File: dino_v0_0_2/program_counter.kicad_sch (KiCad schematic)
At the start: 20 parts, among them U1 74LS193, U10 74LS02, U11 74LS245, U12 74LS245, U13 74LS245, U14 74LS245, U2 74LS193, U3 74LS193, U36 7400, U4 74LS193

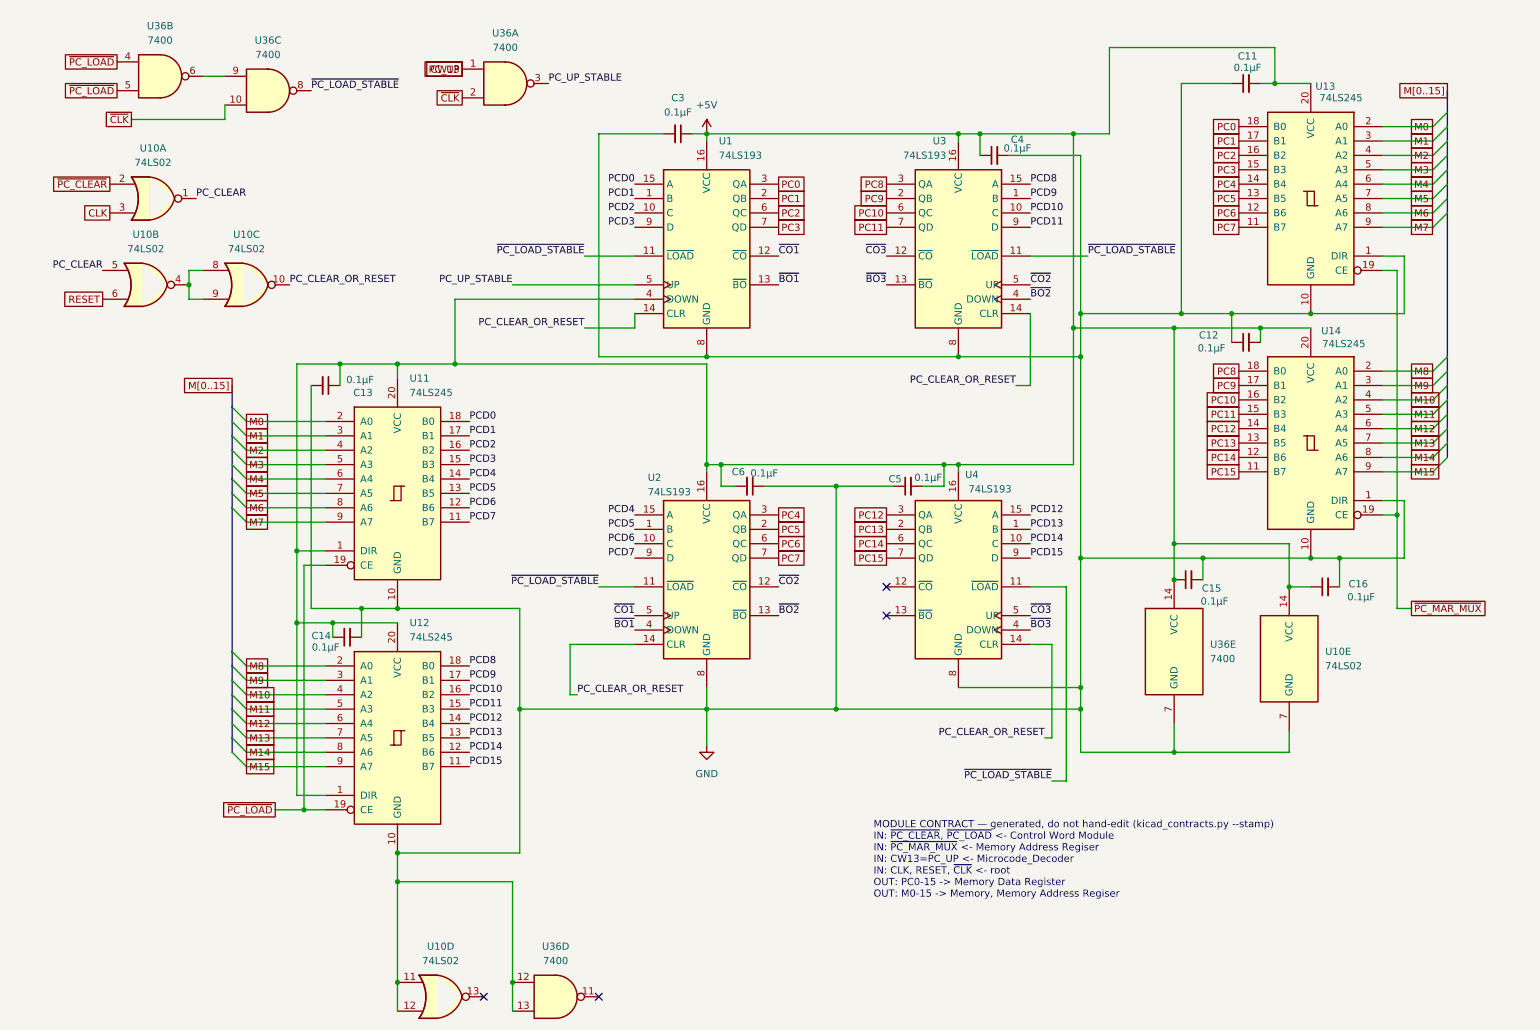
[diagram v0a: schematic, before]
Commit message: feat(int): draw the interrupt block; sheet cleanup pass
New sheet dino_v0_0_2/interrupt.kicad_sch (page 15): U80-U87, R28 4.7k
pull-up on ~{IRQ}, R29 100R on the block's CLK branch, C83-C90. Every
pin per PHASE_INT SECTION 3, checked against the plan with kicad_netlist
and kicad-cli (146 pins, 0 mismatches).

Old sheets (SECTION 3.2): U28.4 lifted off GND to INJECT; U61.3 to
END_OR_ACCEPT; U36.1 to PC_UP_GATED; U49 D0-3 cut from U48 Za-Zd and
routed through U87 as FLAG_NEXT0-3 / FLAG_D0-3; FLAG_C/Z/V/N and the
five decoder outputs made global. dino_serial: U104 74LS05, INTR ->
~{IRQ}, C4.

Placement pass on every sheet: bus entries and global labels no longer
share wires; M, CW, T, IRB and SA buses kept as labelled keys. Nets
diffed against HEAD per sheet: only the intended changes and a rotated
C29. Project ERC: 0 errors. MODULE CONTRACT stamps regenerated.

Co-Authored-By: Claude Fable 5.1 <noreply@anthropic.com>
Claude-Session: https://claude.ai/code/session_01JGxSS4MVUcaZdKZGtKroSg
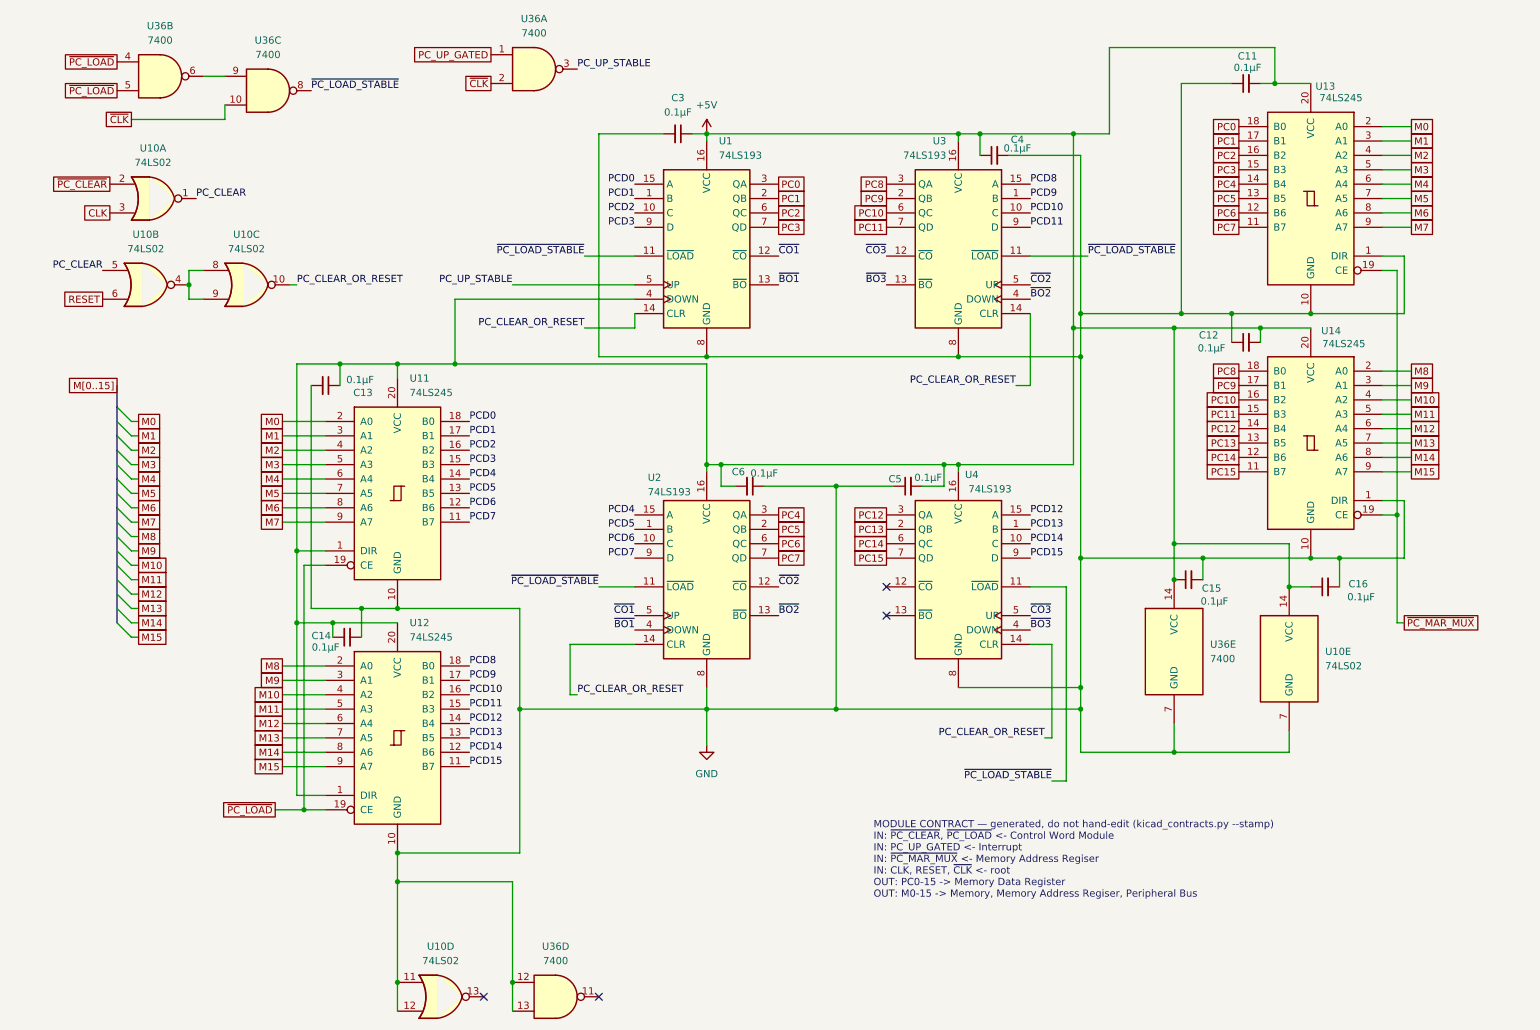
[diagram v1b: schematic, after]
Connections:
- net CW13 renamed PC_UP_GATED
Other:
- note added: "MODULE CONTRACT — generated, do not hand-edit (kicad_contracts.py --stamp) IN: ~{PC_CLEAR}, ~{PC_LOAD} <- Control Word Module IN: PC_UP_GATED <- Interrupt IN: ~{PC_MAR_MUX} <- Memory Address Regiser IN: CLK, RESET, ~{CLK} <- root OUT: PC0-15 -> Memory Data Register OUT: M0-15 -> Memory, Memory Address Regiser, Peripheral Bus"
- note removed: "MODULE CONTRACT — generated, do not hand-edit (kicad_contracts.py --stamp) IN: ~{PC_CLEAR}, ~{PC_LOAD} <- Control Word Module IN: ~{PC_MAR_MUX} <- Memory Address Regiser IN: CW13=PC_UP <- Microcode_Decoder IN: CLK, RESET, ~{CLK} <- root OUT: PC0-15 -> Memory Data Register OUT: M0-15 -> Memory, Memory Address Regiser"
- moved on the sheet: U36A

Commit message: feat(pcb): Rev 1.0 pre-order batch, debug access, no fuse
From the five-way pre-order review:

- Debug: J14 clock select at U27.3 (1.024 MHz / 512k / 256k / 128k /
  STEP), STEP debounced from SW3 through the spare U56 5->6 Schmitt;
  J15 LA header (16 control signals, a GND beside each); J16 power for
  the OB LEDs; DNP cap pads C94/C95/C96 on CLK at U6.2, CLK_ALU at
  U47.11 and CW15 (HALT) at U61.5; 15 GND scope loops so every IC but
  two is within 50 mm of one, plus a +5V test point.
- Power: F1 removed, no fuse (Rico); J9's +5V solid to the plane;
  bulk C97-C100 100 uF spread across the board; C92 ceramic.
- Layout: U6 beside U27 (its CLK pin was 138 mm out on raw CLK), C1/R1
  beside U56, RST_SIG in RESET and CLK_R / CLK_INT / CLK_M / CLK_SEL in
  CLK, thermal gap 0.3 mm (GND plane slots from 25 mm to under 8 mm),
  tracks >= 0.2 mm with no neckdown (6/6 mil tier), board min track rule.
- Values to match the bench: U56 SN7414N, U36 74LS00, U51 DM7400N,
  Y1 4.096 MHz.
- Edge socket: silk outline and a pin-1 arrow (unkeyed; a reversed card
  shorts +5V).

Re-routed by Freerouting 2.5.0 from an empty board. KiCad DRC 0
unconnected / 0 errors, schematic parity 0, one text_thickness warning
on the TrueType board text; ERC at its 74 baseline; test_pcb_envelope
7/7. Clock copper: CLK 296 mm, ~{CLK} 283, CLK_B 162, CLK_ALU 48.
Fab: fabrication/dino_rev_1_0_gerbers_20261029_1153.zip.

Co-Authored-By: Claude Opus 5.5 <noreply@anthropic.com>
Claude-Session: https://claude.ai/code/session_01JGxSS4MVUcaZdKZGtKroSg
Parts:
- U36: value 7400 -> 74LS00
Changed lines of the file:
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@@
 			)
 		)
-		(property "Value" "7400"
+		(property "Value" "74LS00"
 			(at 52.0617 21.59 0)
 			(show_name no)
@@
 			)
 		)
-		(property "Value" "7400"
+		(property "Value" "74LS00"
 			(at 102.8617 181.61 0)
 			(show_name no)
@@
 			)
 		)
-		(property "Value" "7400"
+		(property "Value" "74LS00"
 			(at 33.0117 19.05 0)
 			(show_name no)
@@
 			)
 		)
-		(property "Value" "7400"
+		(property "Value" "74LS00"
 			(at 218.44 128.2699 0)
 			(show_name no)
@@
 			)
 		)
-		(property "Value" "7400"
+		(property "Value" "74LS00"
 			(at 99.0517 17.78 0)
 			(show_name no)
